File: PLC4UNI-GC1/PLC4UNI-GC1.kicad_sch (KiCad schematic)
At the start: 7 parts

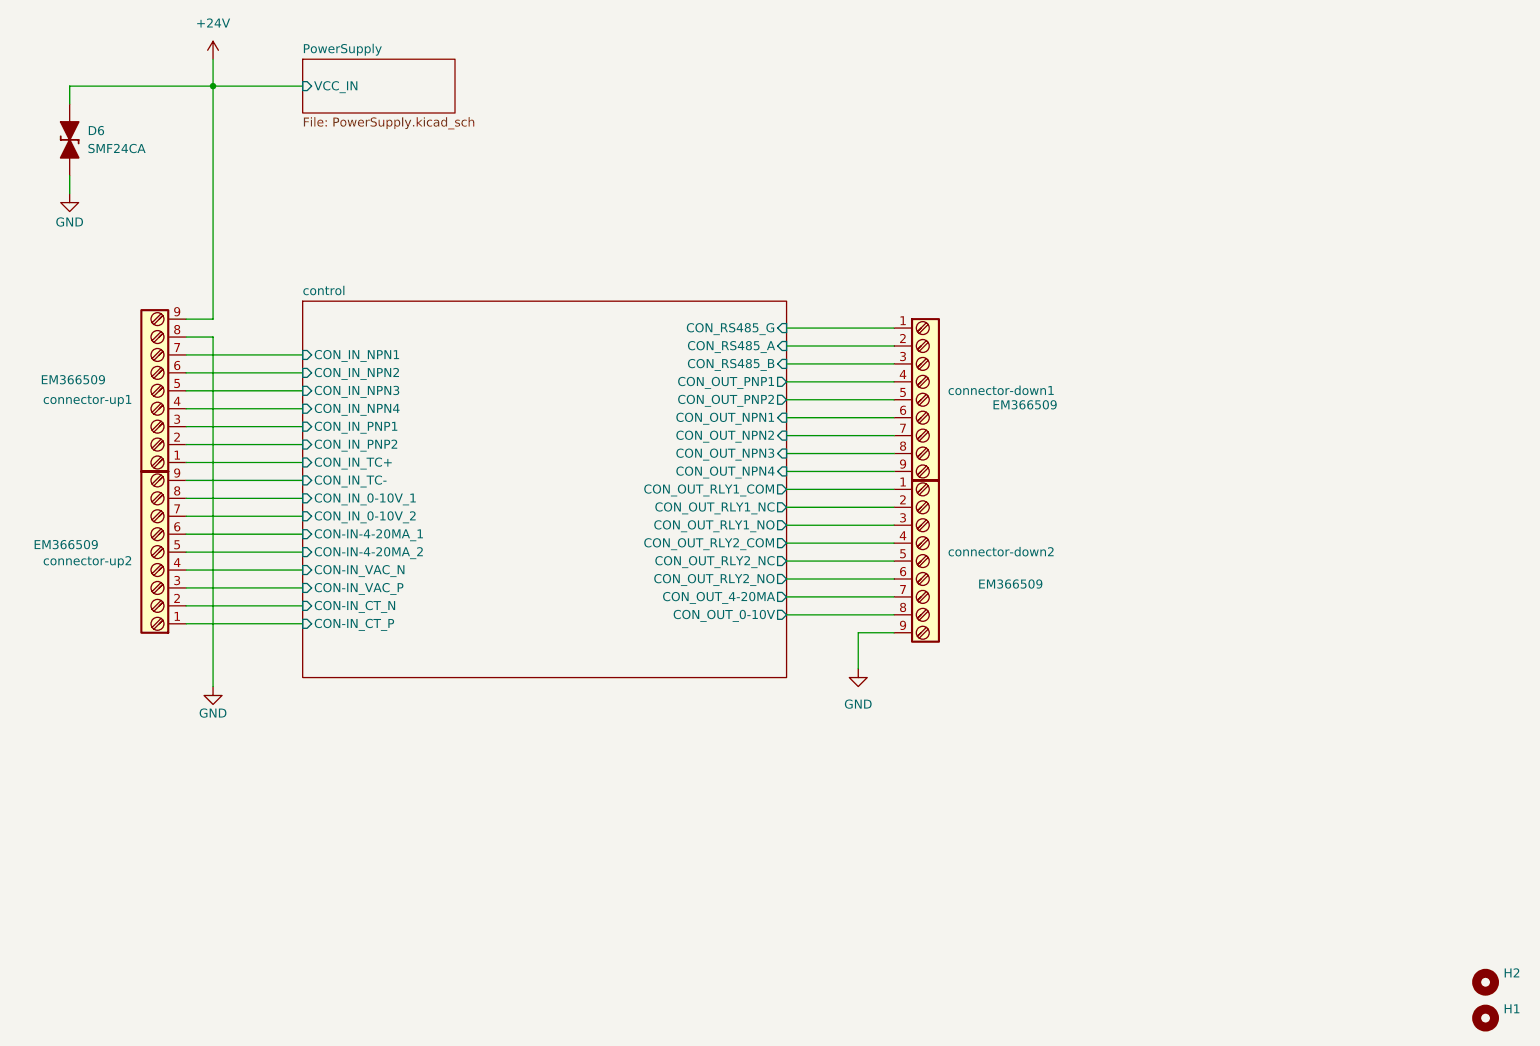
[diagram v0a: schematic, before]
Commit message: Colocadas el 80% de las piezas
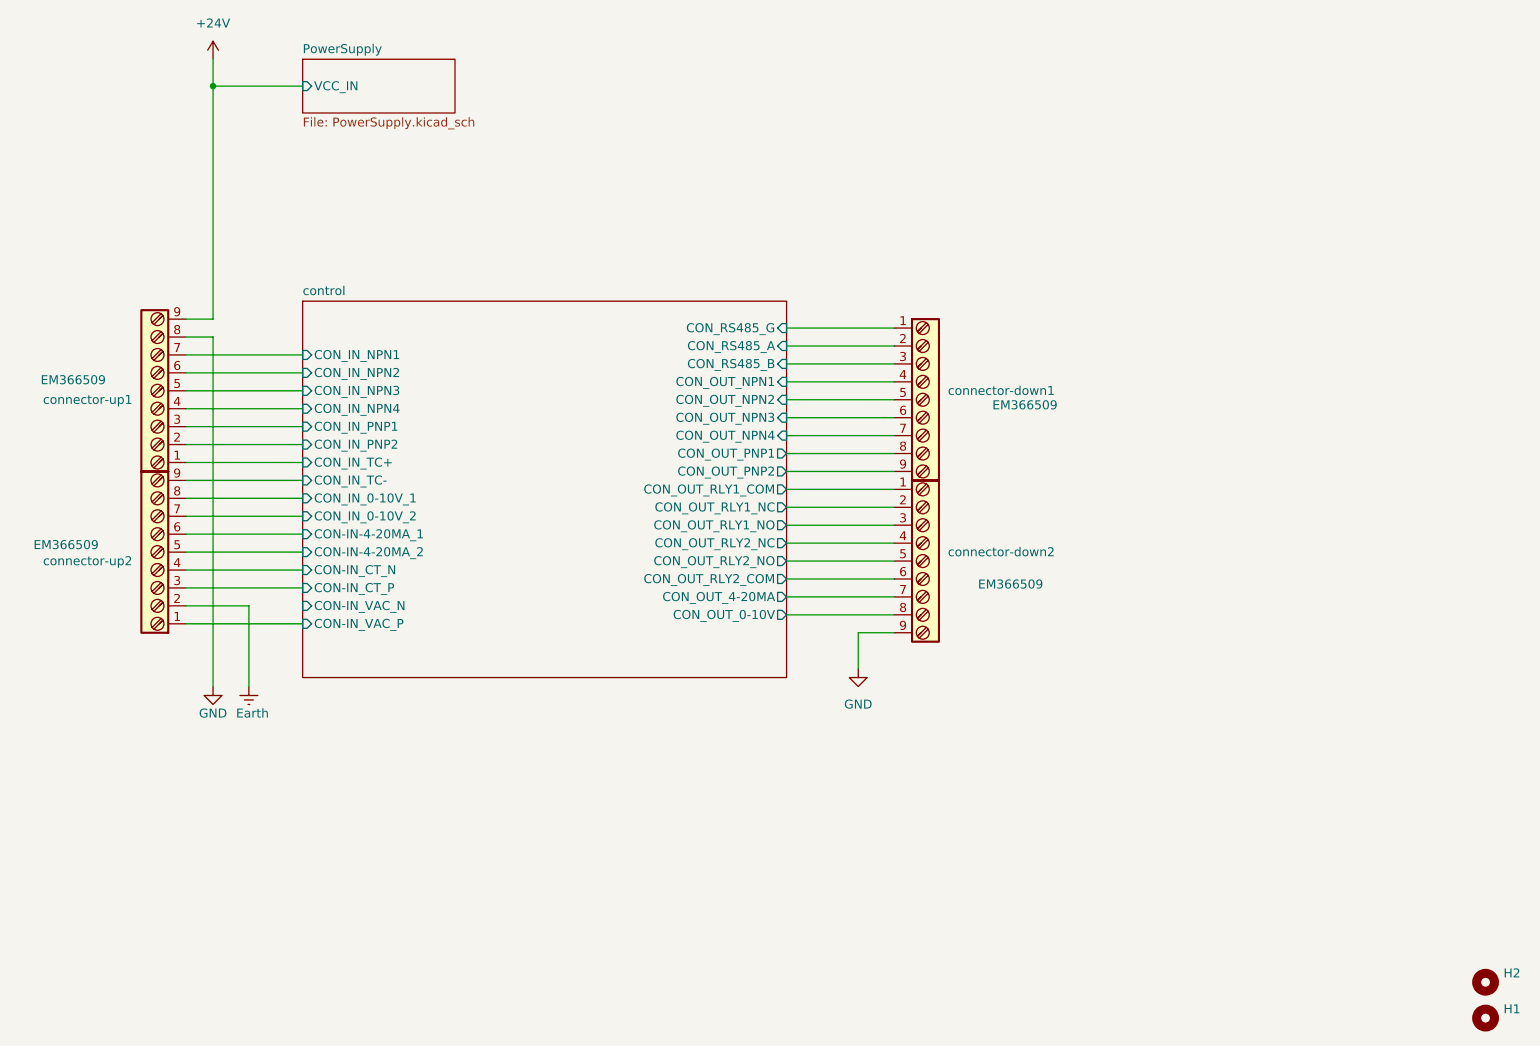
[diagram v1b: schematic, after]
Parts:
- removed D6: SMF24CA, Diode_SMD_AKL:D_SOD-123F, symbol Diode_TVS_AKL:SMF24CA
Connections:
- net control/CON-IN_CT_N: now also connector-up2.4; no longer connector-up2.2
- net control/CON-IN_CT_P: now also connector-up2.3; no longer connector-up2.1
- net control/CON-IN_VAC_N: no longer connector-up2.4
- net control/CON-IN_VAC_P: now also connector-up2.1; no longer connector-up2.3
- net control/CON_OUT_NPN1: now also connector-down1.4; no longer connector-down1.6
- net control/CON_OUT_NPN2: now also connector-down1.5; no longer connector-down1.7
- net control/CON_OUT_NPN3: now also connector-down1.6; no longer connector-down1.8
- net control/CON_OUT_NPN4: now also connector-down1.7; no longer connector-down1.9
- net control/CON_OUT_PNP1: now also connector-down1.8; no longer connector-down1.4
- net control/CON_OUT_PNP2: now also connector-down1.9; no longer connector-down1.5
- net control/CON_OUT_RLY2_COM: now also connector-down2.6; no longer connector-down2.4
- net control/CON_OUT_RLY2_NC: now also connector-down2.4; no longer connector-down2.5
- net control/CON_OUT_RLY2_NO: now also connector-down2.5; no longer connector-down2.6
- new net Earth: connector-up2.2
